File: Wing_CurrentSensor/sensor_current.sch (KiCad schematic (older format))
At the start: 20 parts, among them J1 feather long, J2 feather short, J3 PJ-320B, J4 Analog Selection, U1 TL084, U2 AD8226

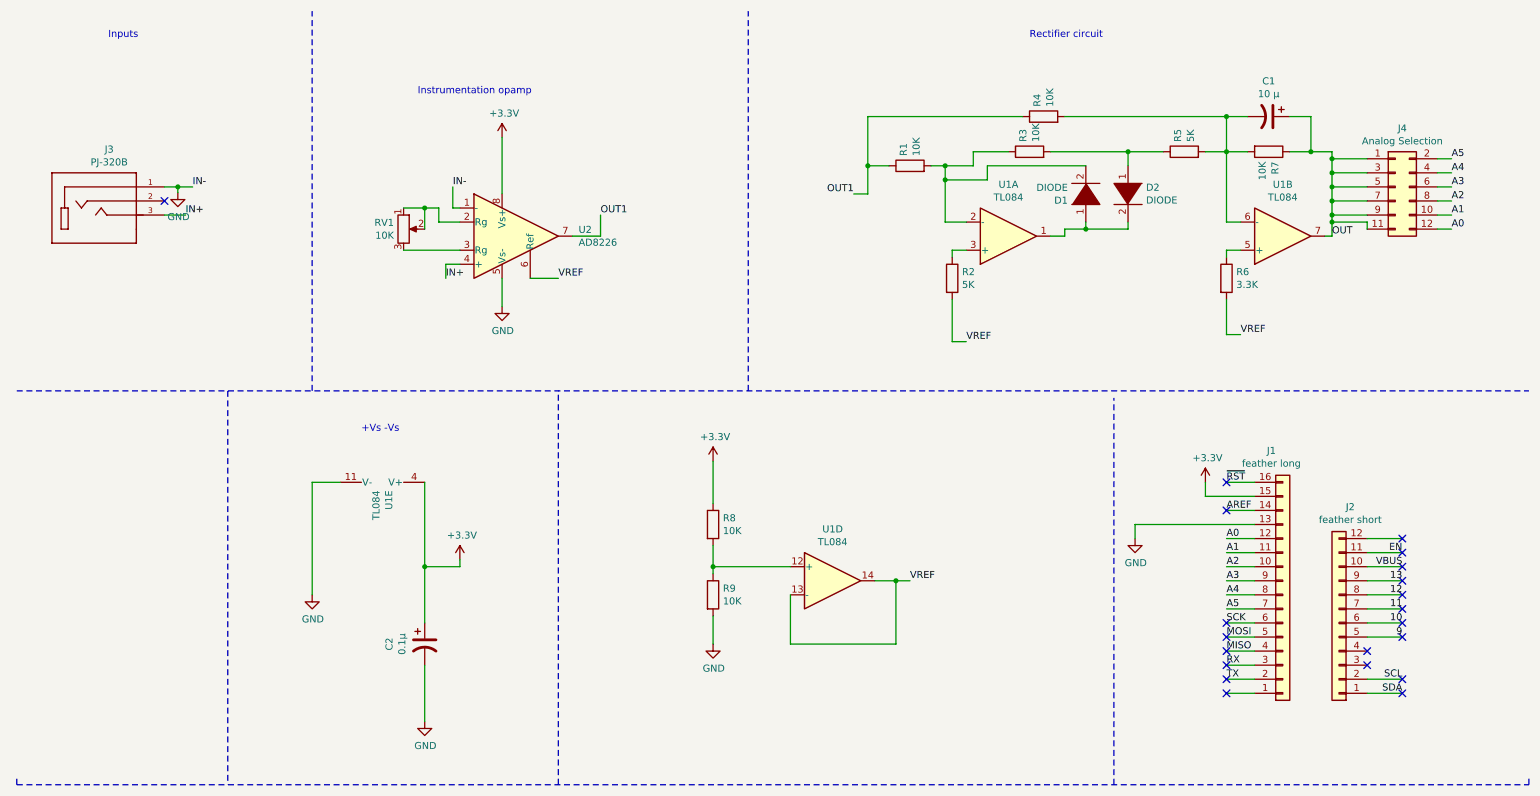
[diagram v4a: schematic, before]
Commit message: Change_name_add connector
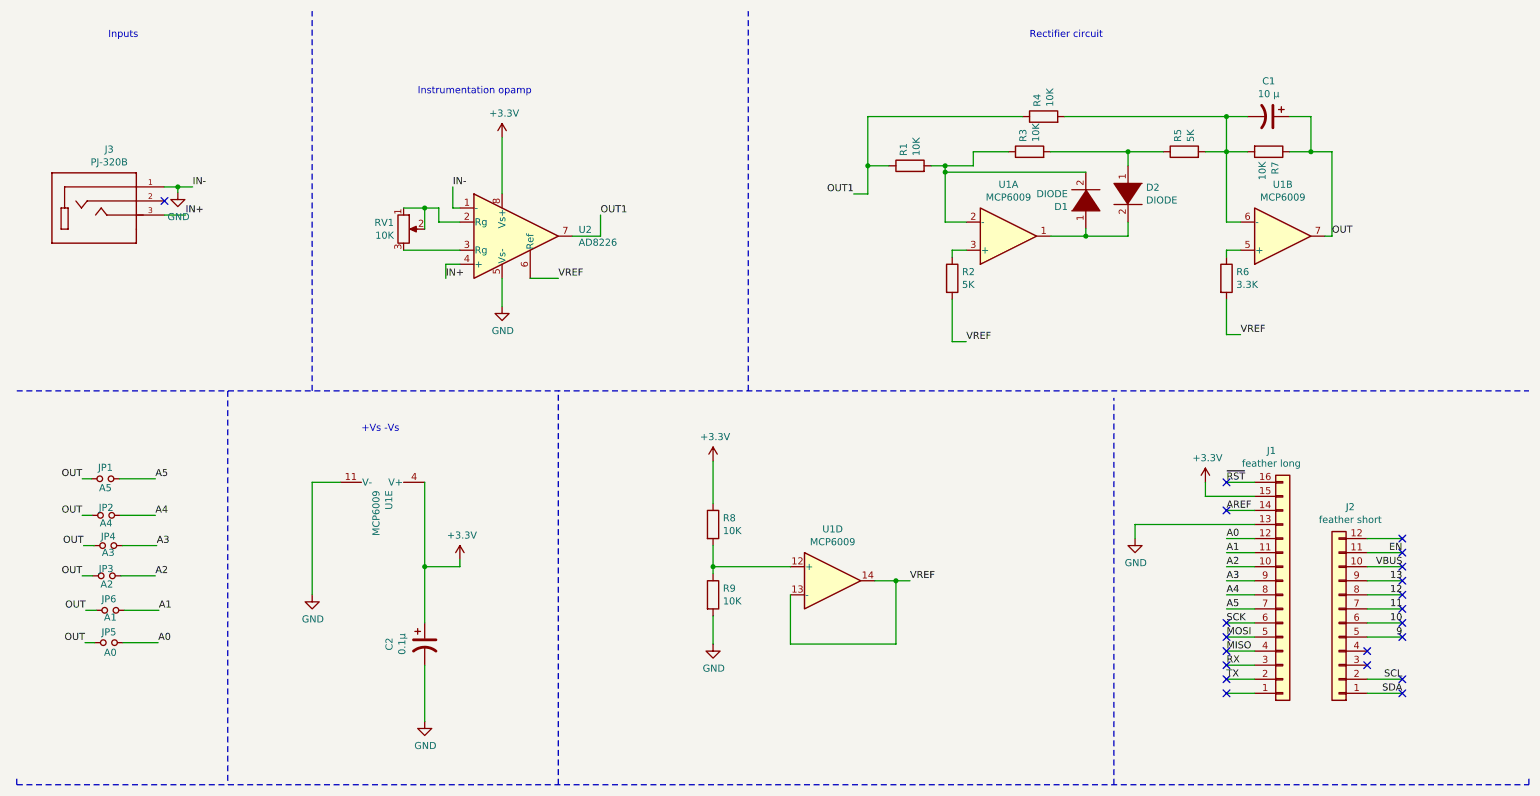
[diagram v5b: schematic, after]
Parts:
- removed J4: Analog Selection, Connector_PinHeader_2.54mm:PinHeader_2x06_P2.54mm_Vertical, symbol Connector_Generic:Conn_02x06_Odd_Even
- added JP1: A5, Jumper:SolderJumper-2_P1.3mm_Open_TrianglePad1.0x1.5mm, symbol Device:Jumper_NO_Small
- added JP2: A4, Jumper:SolderJumper-2_P1.3mm_Open_TrianglePad1.0x1.5mm, symbol Device:Jumper_NO_Small
- added JP3: A2, Jumper:SolderJumper-2_P1.3mm_Open_TrianglePad1.0x1.5mm, symbol Device:Jumper_NO_Small
- added JP4: A3, Jumper:SolderJumper-2_P1.3mm_Open_TrianglePad1.0x1.5mm, symbol Device:Jumper_NO_Small
- added JP5: A0, Jumper:SolderJumper-2_P1.3mm_Open_TrianglePad1.0x1.5mm, symbol Device:Jumper_NO_Small
- added JP6: A1, Jumper:SolderJumper-2_P1.3mm_Open_TrianglePad1.0x1.5mm, symbol Device:Jumper_NO_Small
- U1: value TL084 -> MCP6009
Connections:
- net A0: now also JP5.2
- net A1: now also JP6.2
- net A2: now also JP3.2
- net A3: now also JP4.2
- net A4: now also JP2.2
- net A5: now also JP1.2
- net OUT: now also JP1.1, JP2.1, JP3.1, JP4.1, JP5.1, JP6.1
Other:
- moved on the sheet: D1
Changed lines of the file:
@@
 P 3050 3900
 F 0 "U1" H 3008 3946 50  0000 L CNN
-F 1 "TL084" H 3008 3855 50  0000 L CNN
+F 1 "MCP6009" H 3008 3855 50  0000 L CNN
 F 2 "Package_SO:SO-14_3.9x8.65mm_P1.27mm" H 3000 4000 50  0001 C CNN
 F 3 "http://www.ti.com/lit/ds/symlink/tl081.pdf" H 3100 4100 50  0001 C CNN
@@
 	1    0    0    -1
 $EndComp
-Text Label 9800 2050 0    50   ~ 0
+Text Label 9800 2045 0    50   ~ 0
 OUT
 Wire Wire Line
@@
 $EndComp
 Wire Wire Line
-	8350 2000 8050 2000
-Wire Wire Line
-	8350 1950 8350 2000
-Wire Wire Line
 	8350 1450 8350 1550
 Wire Wire Line
@@
 $EndComp
 Wire Wire Line
-	7350 1650 7050 1650
-Wire Wire Line
-	7350 1550 7350 1650
-Wire Wire Line
-	8050 1550 7350 1550
-Wire Wire Line
-	8050 2000 8050 1950
-Wire Wire Line
-	7050 1550 7050 1650
+	7050 1550 7050 1595
 Wire Wire Line
 	6950 1550 7050 1550
@@
 L sensor_current-rescue:DIODE-pspice D1
 U 1 1 602F1EFE
-P 8050 1750
-F 0 "D1" V 8004 1878 50  0000 L CNN
-F 1 "DIODE" V 8095 1878 50  0000 L CNN
-F 2 "Diode_SMD:D_SOD-323F" H 8050 1750 50  0001 C CNN
-F 3 "~" H 8050 1750 50  0001 C CNN
-	1    8050 1750
+P 8050 1795
+F 0 "D1" V 8004 1923 50  0000 L CNN
+F 1 "DIODE" V 8095 1923 50  0000 L CNN
+F 2 "Diode_SMD:D_SOD-323F" H 8050 1795 50  0001 C CNN
+F 3 "~" H 8050 1795 50  0001 C CNN
+	1    8050 1795
 	0    -1   -1   0
 $EndComp
@@
 +Vs -Vs
 Wire Wire Line
-	7800 2050 7900 2050
-Wire Wire Line
-	7900 2050 7900 2000
-Wire Wire Line
-	7900 2000 8050 2000
-Connection ~ 8050 2000
-Wire Wire Line
 	7200 1950 7050 1950
 Wire Wire Line
-	7050 1950 7050 1650
-Connection ~ 7050 1650
-Wire Wire Line
 	9050 1950 9050 1450
 Wire Wire Line
 	9050 1950 9150 1950
-Wire Wire Line
-	9800 2050 9800 1950
 Wire Wire Line
 	9800 1450 9650 1450
@@
 P 6250 4500
 F 0 "U1" H 6250 4867 50  0000 C CNN
-F 1 "TL084" H 6250 4776 50  0000 C CNN
+F 1 "MCP6009" H 6250 4776 50  0000 C CNN
 F 2 "Package_SO:SO-14_3.9x8.65mm_P1.27mm" H 6200 4600 50  0001 C CNN
 F 3 "http://www.ti.com/lit/ds/symlink/tl081.pdf" H 6300 4700 50  0001 C CNN
@@
 P 9450 2050
 F 0 "U1" H 9450 1683 50  0000 C CNN
-F 1 "TL084" H 9450 1774 50  0000 C CNN
+F 1 "MCP6009" H 9450 1774 50  0000 C CNN
 F 2 "Package_SO:SO-14_3.9x8.65mm_P1.27mm" H 9400 2150 50  0001 C CNN
 F 3 "http://www.ti.com/lit/ds/symlink/tl081.pdf" H 9500 2250 50  0001 C CNN
@@
 P 7500 2050
 F 0 "U1" H 7500 1683 50  0000 C CNN
-F 1 "TL084" H 7500 1774 50  0000 C CNN
+F 1 "MCP6009" H 7500 1774 50  0000 C CNN
 F 2 "Package_SO:SO-14_3.9x8.65mm_P1.27mm" H 7450 2150 50  0001 C CNN
 F 3 "http://www.ti.com/lit/ds/symlink/tl081.pdf" H 7550 2250 50  0001 C CNN
@@
 NoConn ~ 10300 4600
 NoConn ~ 10300 4500
-Connection ~ 9800 1500
-Wire Wire Line
-	9800 1500 9800 1450
-Connection ~ 9800 1600
-Wire Wire Line
-	9800 1600 9800 1500
-Connection ~ 9800 1700
-Wire Wire Line
-	9800 1700 9800 1600
 Wire Wire Line
 	3900 2350 3900 2550
@@
 NoConn ~ 9050 4000
 NoConn ~ 9050 3800
-Connection ~ 9800 1800
-Wire Wire Line
-	9800 1800 9800 1700
-Connection ~ 9800 1900
-Wire Wire Line
-	9800 1900 9800 1800
-Wire Wire Line
-	9800 1500 10050 1500
-Wire Wire Line
-	9800 1600 10050 1600
-Wire Wire Line
-	9800 1700 10050 1700
-Wire Wire Line
-	9800 1800 10050 1800
-Wire Wire Line
-	9800 1900 10050 1900
-Wire Wire Line
-	10050 2000 10050 1950
-Wire Wire Line
-	10050 1950 9800 1950
-Connection ~ 9800 1950
-Wire Wire Line
-	9800 1950 9800 1900
-Text Label 10650 2000 0    50   ~ 0
+Text Label 1455 4940 0    50   ~ 0
 A0
-Text Label 10650 1900 0    50   ~ 0
+Text Label 1460 4710 0    50   ~ 0
 A1
-Text Label 10650 1800 0    50   ~ 0
+Text Label 1435 4465 0    50   ~ 0
 A2
-Text Label 10650 1700 0    50   ~ 0
+Text Label 1445 4250 0    50   ~ 0
 A3
-Text Label 10650 1600 0    50   ~ 0
+Text Label 1435 4035 0    50   ~ 0
 A4
-Text Label 10650 1500 0    50   ~ 0
+Text Label 1435 3775 0    50   ~ 0
 A5
-Wire Wire Line
-	10550 2000 10650 2000
-Wire Wire Line
-	10550 1900 10650 1900
-Wire Wire Line
-	10550 1800 10650 1800
-Wire Wire Line
-	10550 1700 10650 1700
-Wire Wire Line
-	10550 1600 10650 1600
-Wire Wire Line
-	10550 1500 10650 1500
 Wire Notes Line
 	1950 3150 1950 5950
@@
 	3900 1350 3900 1750
 $Comp
-L Connector_Generic:Conn_02x06_Odd_Even J4
-U 1 1 604C74A8
-P 10250 1700
-F 0 "J4" H 10300 2117 50  0000 C CNN
-F 1 "Analog Selection" H 10300 2026 50  0000 C CNN
-F 2 "Connector_PinHeader_2.54mm:PinHeader_2x06_P2.54mm_Vertical" H 10250 1700 50  0001 C CNN
-F 3 "~" H 10250 1700 50  0001 C CNN
-	1    10250 1700
-	1    0    0    -1
-$EndComp
-$Comp
 L power:GND #PWR0108
 U 1 1 60D403E1
@@
 Wire Wire Line
 	1595 1700 1700 1700
+Wire Wire Line
+	8350 2050 8050 2050
+Wire Wire Line
+	8350 1950 8350 2050
+Connection ~ 8050 2050
+Wire Wire Line
+	7800 2050 8050 2050
+Wire Wire Line
+	8050 1995 8050 2050
+Connection ~ 7050 1595
+Wire Wire Line
+	7050 1595 7050 1950
+Wire Wire Line
+	7050 1595 8050 1595
+$Comp
+L Device:Jumper_NO_Small JP2
+U 1 1 60FA6350
+P 1085 4035
+F 0 "JP2" H 1085 4090 50  0000 C CNN
+F 1 "A4" H 1085 3980 50  0000 C CNN
+F 2 "Jumper:SolderJumper-2_P1.3mm_Open_TrianglePad1.0x1.5mm" H 1085 4035 50  0001 C CNN
+F 3 "~" H 1085 4035 50  0001 C CNN
+	1    1085 4035
+	1    0    0    -1
+$EndComp
+$Comp
+L Device:Jumper_NO_Small JP5
+U 1 1 60FA6D93
+P 1105 4940
+F 0 "JP5" H 1105 5015 50  0000 C CNN
+F 1 "A0" H 1115 4870 50  0000 C CNN
+F 2 "Jumper:SolderJumper-2_P1.3mm_Open_TrianglePad1.0x1.5mm" H 1105 4940 50  0001 C CNN
+F 3 "~" H 1105 4940 50  0001 C CNN
+	1    1105 4940
+	1    0    0    -1
+$EndComp
+$Comp
+L Device:Jumper_NO_Small JP1
+U 1 1 60FA70DF
+P 1080 3775
+F 0 "JP1" H 1080 3855 50  0000 C CNN
+F 1 "A5" H 1080 3710 50  0000 C CNN
+F 2 "Jumper:SolderJumper-2_P1.3mm_Open_TrianglePad1.0x1.5mm" H 1080 3775 50  0001 C CNN
+F 3 "~" H 1080 3775 50  0001 C CNN
+	1    1080 3775
+	1    0    0    -1
+$EndComp
+$Comp
+L Device:Jumper_NO_Small JP4
+U 1 1 60FA73E6
+P 1100 4250
+F 0 "JP4" H 1100 4315 50  0000 C CNN
+F 1 "A3" H 1100 4200 50  0000 C CNN
+F 2 "Jumper:SolderJumper-2_P1.3mm_Open_TrianglePad1.0x1.5mm" H 1100 4250 50  0001 C CNN
+F 3 "~" H 1100 4250 50  0001 C CNN
+	1    1100 4250
+	1    0    0    -1
+$EndComp
+$Comp
+L Device:Jumper_NO_Small JP3
+U 1 1 60FA78D6
+P 1090 4465
+F 0 "JP3" H 1085 4515 50  0000 C CNN
+F 1 "A2" H 1090 4405 50  0000 C CNN
+F 2 "Jumper:SolderJumper-2_P1.3mm_Open_TrianglePad1.0x1.5mm" H 1090 4465 50  0001 C CNN
+F 3 "~" H 1090 4465 50  0001 C CNN
+	1    1090 4465
+	1    0    0    -1
+$EndComp
+$Comp
+L Device:Jumper_NO_Small JP6
+U 1 1 60FA7B5D
+P 1115 4710
+F 0 "JP6" H 1105 4790 50  0000 C CNN
+F 1 "A1" H 1115 4660 50  0000 C CNN
+F 2 "Jumper:SolderJumper-2_P1.3mm_Open_TrianglePad1.0x1.5mm" H 1115 4710 50  0001 C CNN
+F 3 "~" H 1115 4710 50  0001 C CNN
+	1    1115 4710
+	1    0    0    -1
+$EndComp
+Wire Wire Line
+	1180 3775 1435 3775
+Wire Wire Line
+	1185 4035 1435 4035
+Wire Wire Line
+	1200 4250 1445 4250
+Wire Wire Line
+	1190 4465 1435 4465
+Wire Wire Line
+	1215 4710 1460 4710
+Wire Wire Line
+	1205 4940 1455 4940
+Wire Wire Line
+	9800 1450 9800 2050
+Text Label 915  3775 2    50   ~ 0
+OUT
+Text Label 915  4035 2    50   ~ 0
+OUT
+Text Label 925  4250 2    50   ~ 0
+OUT
+Text Label 915  4465 2    50   ~ 0
+OUT
+Text Label 940  4710 2    50   ~ 0
+OUT
+Text Label 935  4940 2    50   ~ 0
+OUT
+Wire Wire Line
+	935  4940 1005 4940
+Wire Wire Line
+	940  4710 1015 4710
+Wire Wire Line
+	915  4465 990  4465
+Wire Wire Line
+	925  4250 1000 4250
+Wire Wire Line
+	915  4035 985  4035
+Wire Wire Line
+	915  3775 980  3775
 $EndSCHEMATC

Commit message: Add_labels
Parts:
- C1, C2: symbol sensor_current-rescue:CP1-Device -> sensor_current-rescue:CP1-Device-sensor_current-rescue
- D1, D2: symbol sensor_current-rescue:DIODE-pspice -> sensor_current-rescue:DIODE-pspice-sensor_current-rescue
- J1: symbol sensor_current-rescue:Conn_01x16-Connector_Generic -> sensor_current-rescue:Conn_01x16-Connector_Generic-sensor_current-rescue
- J2: symbol sensor_current-rescue:Conn_01x12-Connector_Generic -> sensor_current-rescue:Conn_01x12-Connector_Generic-sensor_current-rescue
- J3: symbol sensor_current-rescue:SJ-3524-SMT-jack -> sensor_current-rescue:SJ-3524-SMT-jack-sensor_current-rescue
- R1, R2, R3, R4, R5, R6, R7, R8, R9: symbol sensor_current-rescue:R-Device -> sensor_current-rescue:R-Device-sensor_current-rescue
- RV1: symbol sensor_current-rescue:R_POT-Device -> sensor_current-rescue:R_POT-Device-sensor_current-rescue
- U1: symbol sensor_current-rescue:TL084-Amplifier_Operational -> sensor_current-rescue:TL084-Amplifier_Operational-sensor_current-rescue
- U2: symbol sensor_current-rescue:AD8421-Amplifier_Instrumentation -> sensor_current-rescue:AD8421-Amplifier_Instrumentation-sensor_current-rescue
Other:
- note added: "Analog Inputs"
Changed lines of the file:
@@
 	3350 3800 3350 4400
 $Comp
-L sensor_current-rescue:CP1-Device C2
+L sensor_current-rescue:CP1-Device-sensor_current-rescue C2
 U 1 1 601E5B1F
 P 3350 4950
@@
 $EndComp
 $Comp
-L sensor_current-rescue:TL084-Amplifier_Operational U1
+L sensor_current-rescue:TL084-Amplifier_Operational-sensor_current-rescue U1
 U 5 1 601E5B25
 P 3050 3900
@@
 $EndComp
 $Comp
-L sensor_current-rescue:GND-power #PWR0102
+L sensor_current-rescue:GND-power-sensor_current-rescue #PWR0102
 U 1 1 60295F05
 P 3350 5500
@@
 	7200 2150 7100 2150
 $Comp
-L sensor_current-rescue:R-Device R2
+L sensor_current-rescue:R-Device-sensor_current-rescue R2
 U 1 1 602E05A9
 P 7100 2350
@@
 	9050 2200 9050 2150
 $Comp
-L sensor_current-rescue:R-Device R6
+L sensor_current-rescue:R-Device-sensor_current-rescue R6
 U 1 1 602E8C25
 P 9050 2350
@@
 	9200 1450 9050 1450
 $Comp
-L sensor_current-rescue:R-Device R7
+L sensor_current-rescue:R-Device-sensor_current-rescue R7
 U 1 1 602F1EB7
 P 9350 1450
@@
 	9200 1200 9050 1200
 $Comp
-L sensor_current-rescue:CP1-Device C1
+L sensor_current-rescue:CP1-Device-sensor_current-rescue C1
 U 1 1 602F1EBF
 P 9350 1200
@@
 	6500 1200 7600 1200
 $Comp
-L sensor_current-rescue:R-Device R4
+L sensor_current-rescue:R-Device-sensor_current-rescue R4
 U 1 1 602F1EC9
 P 7750 1200
@@
 	8600 1450 8350 1450
 $Comp
-L sensor_current-rescue:R-Device R5
+L sensor_current-rescue:R-Device-sensor_current-rescue R5
 U 1 1 602F1ED1
 P 8750 1450
@@
 	7050 1550 7250 1550
 $Comp
-L sensor_current-rescue:R-Device R3
+L sensor_current-rescue:R-Device-sensor_current-rescue R3
 U 1 1 602F1EE8
 P 7650 1450
@@
 	6950 1550 7050 1550
 $Comp
-L sensor_current-rescue:DIODE-pspice D1
+L sensor_current-rescue:DIODE-pspice-sensor_current-rescue D1
 U 1 1 602F1EFE
 P 8050 1795
@@
 $EndComp
 $Comp
-L sensor_current-rescue:R-Device R1
+L sensor_current-rescue:R-Device-sensor_current-rescue R1
 U 1 1 602F1F0A
 P 6800 1550
@@
 	8250 5950 8250 3200
 $Comp
-L sensor_current-rescue:R-Device R8
+L sensor_current-rescue:R-Device-sensor_current-rescue R8
 U 1 1 60371C97
 P 5400 4100
@@
 $EndComp
 $Comp
-L sensor_current-rescue:R-Device R9
+L sensor_current-rescue:R-Device-sensor_current-rescue R9
 U 1 1 60372648
 P 5400 4600
@@
 $EndComp
 $Comp
-L sensor_current-rescue:GND-power #PWR0101
+L sensor_current-rescue:GND-power-sensor_current-rescue #PWR0101
 U 1 1 6037A08F
 P 5400 4950
@@
 VREF
 $Comp
-L sensor_current-rescue:GND-power #PWR0103
+L sensor_current-rescue:GND-power-sensor_current-rescue #PWR0103
 U 1 1 603897CB
 P 3900 2550
@@
 	3350 5100 3350 5500
 $Comp
-L sensor_current-rescue:GND-power #PWR0104
+L sensor_current-rescue:GND-power-sensor_current-rescue #PWR0104
 U 1 1 603A380E
 P 2550 4600
@@
 	2550 3800 2550 4600
 $Comp
-L sensor_current-rescue:TL084-Amplifier_Operational U1
+L sensor_current-rescue:TL084-Amplifier_Operational-sensor_current-rescue U1
 U 4 1 60375049
 P 6250 4500
@@
 	5400 4400 5400 4450
 $Comp
-L sensor_current-rescue:TL084-Amplifier_Operational U1
+L sensor_current-rescue:TL084-Amplifier_Operational-sensor_current-rescue U1
 U 2 1 602E8C1B
 P 9450 2050
@@
 $EndComp
 $Comp
-L sensor_current-rescue:TL084-Amplifier_Operational U1
+L sensor_current-rescue:TL084-Amplifier_Operational-sensor_current-rescue U1
 U 1 1 602E05B2
 P 7500 2050
@@
 	9050 2750 9150 2750
 $Comp
-L sensor_current-rescue:Conn_01x16-Connector_Generic J1
+L sensor_current-rescue:Conn_01x16-Connector_Generic-sensor_current-rescue J1
 U 1 1 5D375C76
 P 9450 4600
@@
 $EndComp
 $Comp
-L sensor_current-rescue:Conn_01x12-Connector_Generic J2
+L sensor_current-rescue:Conn_01x12-Connector_Generic-sensor_current-rescue J2
 U 1 1 5D375CC4
 P 9850 4800
@@
 	10050 5300 10300 5300
 $Comp
-L sensor_current-rescue:+3.3V-power #PWR01
+L sensor_current-rescue:+3.3V-power-sensor_current-rescue #PWR01
 U 1 1 5D37877D
 P 8900 3800
@@
 $EndComp
 $Comp
-L sensor_current-rescue:GND-power #PWR02
+L sensor_current-rescue:GND-power-sensor_current-rescue #PWR02
 U 1 1 5D3787E4
 P 8400 4200
@@
 	9050 4200 9250 4200
 $Comp
-L sensor_current-rescue:SJ-3524-SMT-jack J3
+L sensor_current-rescue:SJ-3524-SMT-jack-sensor_current-rescue J3
 U 1 1 6040A716
 P 1000 1900
@@
 	4100 2350 4300 2350
 $Comp
-L sensor_current-rescue:AD8421-Amplifier_Instrumentation U2
+L sensor_current-rescue:AD8421-Amplifier_Instrumentation-sensor_current-rescue U2
 U 1 1 602A5CCD
 P 4000 2050
@@
 	1950 3150 1950 5950
 $Comp
-L sensor_current-rescue:DIODE-pspice D2
+L sensor_current-rescue:DIODE-pspice-sensor_current-rescue D2
 U 1 1 602F1EF8
 P 8350 1750
@@
 $EndComp
 $Comp
-L sensor_current-rescue:R_POT-Device RV1
+L sensor_current-rescue:R_POT-Device-sensor_current-rescue RV1
 U 1 1 602A5CBE
 P 3200 2000
@@
 NoConn ~ 10300 4400
 $Comp
-L sensor_current-rescue:+3.3V-power #PWR0105
+L sensor_current-rescue:+3.3V-power-sensor_current-rescue #PWR0105
 U 1 1 604C3DB9
 P 5400 3650
@@
 	5400 3650 5400 3950
 $Comp
-L sensor_current-rescue:+3.3V-power #PWR0106
+L sensor_current-rescue:+3.3V-power-sensor_current-rescue #PWR0106
 U 1 1 604CD61E
 P 3600 4350
@@
 	3600 4400 3350 4400
 $Comp
-L sensor_current-rescue:+3.3V-power #PWR0107
+L sensor_current-rescue:+3.3V-power-sensor_current-rescue #PWR0107
 U 1 1 604DF341
 P 3900 1350
@@
 Wire Wire Line
 	915  3775 980  3775
+Text Notes 915  3320 0    50   ~ 0
+Analog Inputs
 $EndSCHEMATC
